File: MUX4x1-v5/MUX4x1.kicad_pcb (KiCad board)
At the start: 2 copper layers, 94 x 55.9 mm, 28 parts, among them J1 Screw_Terminal_01x02, J12 Conn_01x09_Male, J13 Conn_01x01_Male, J2 Conn_01x09_Male, J3 Conn_01x09_Male, J4 Conn_01x09_Male, J5 Conn_01x09_Male, J6 Conn_01x09_Male, J7 Conn_01x03_Male, U1 74LS153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

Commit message: MUX4:1 v5 in work
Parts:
- added C4: 0.1uF, Capacitor_SMD:C_0805_2012Metric_Pad1.18x1.45mm_HandSolder, F.Cu at (100.3, 134.6)
- added C5: 0.1uF, Capacitor_SMD:C_0805_2012Metric_Pad1.18x1.45mm_HandSolder, F.Cu at (85.1, 134.9)
- moved R1 4.72 mm to (145.4, 116.8), turned to 180 degrees
- moved H3 2.62 mm to (66.0, 155.6)
- moved H1 2.54 mm to (66.0, 109.2)
- moved H4 0.63 mm to (152.4, 155.6)
- moved C2 0.23 mm to (69.8, 133.6)
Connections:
- J7 pad 1: /S0 -> /S1
- J7 pad 2: /S1 -> /S0
- R2 pad 2: /S0 -> /S1
- R3 pad 2: /S1 -> /S0
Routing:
- net GND: track 0.00 -> 338.5 mm, vias 0 -> 1
- net VCC: track 0.00 -> 199.0 mm, vias 0 -> 5
- net /~E: track 0.00 -> 116.2 mm
- net /S1: track 0.00 -> 107.5 mm
- net /S0: track 0.00 -> 105.4 mm
- net /O0: track 0.00 -> 82.6 mm
- net /O2: track 0.00 -> 71.0 mm
- net /O1: track 0.00 -> 69.5 mm
- net /O3: track 0.00 -> 55.1 mm
- net /O4: track 0.00 -> 55.0 mm
- net /O5: track 0.00 -> 40.8 mm
- net /O6: track 0.00 -> 40.7 mm
- net /D7: track 0.00 -> 40.1 mm
- net /D0: track 0.00 -> 37.8 mm
- net /C7: track 0.00 -> 37.3 mm
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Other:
- board size 94 x 55.9 mm -> 96.5 x 56.5 mm

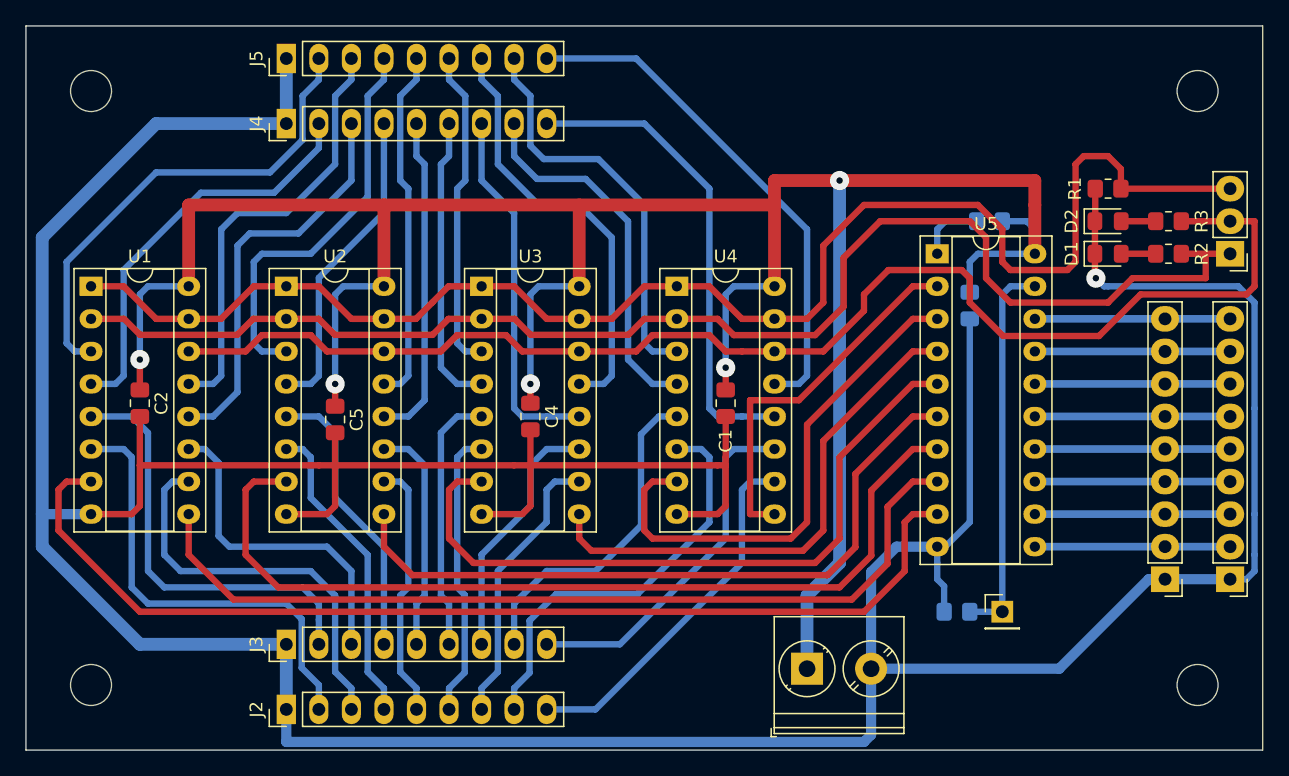
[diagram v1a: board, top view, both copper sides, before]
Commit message: MUX4:1 v5 polishing
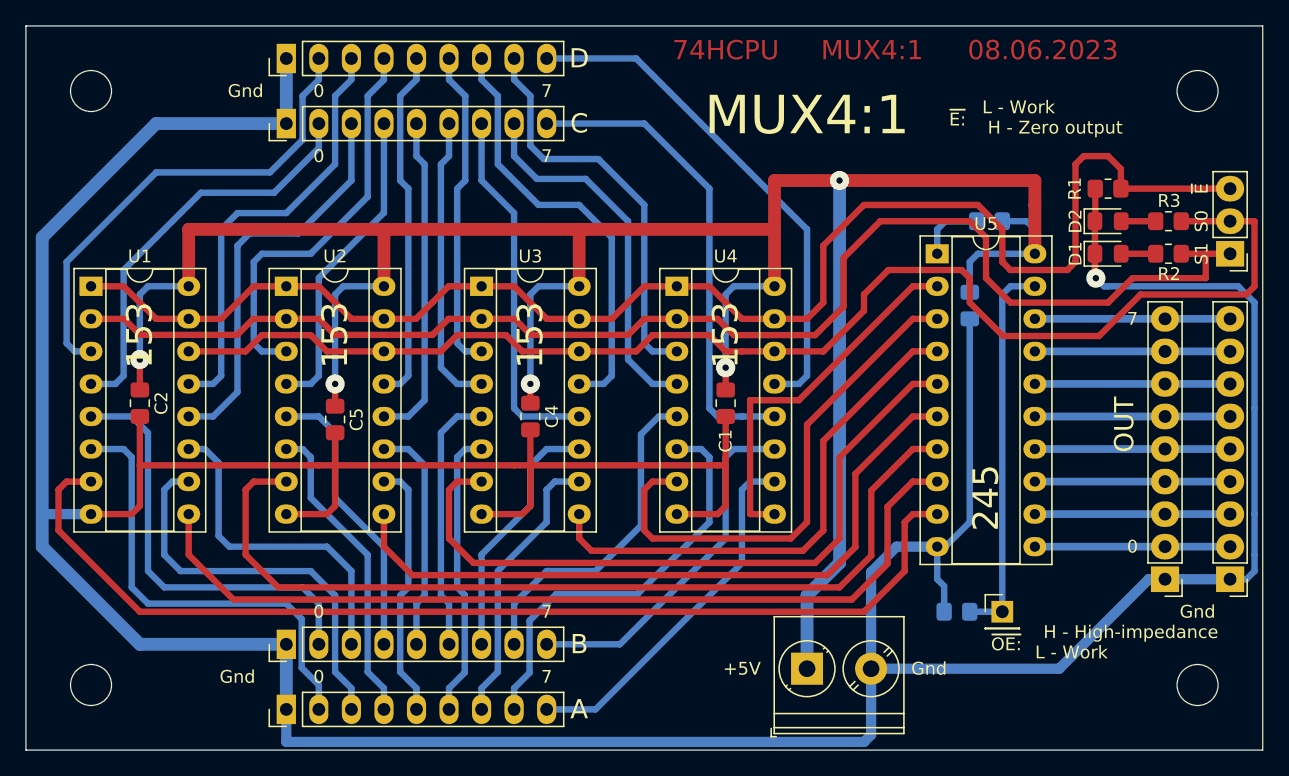
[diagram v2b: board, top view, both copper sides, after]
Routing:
- net VCC: track 199.0 -> 193.3 mm
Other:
- board text added: "+5V"
- board text added: "0"
- board text added: "08.06.2023"
- board text added: "153"
- board text added: "245"
- board text added: "7"
- board text added: "74HCPU"
- board text added: "A"
- board text added: "B"
- board text added: "C"
- board text added: "D"
- board text added: "Gnd"
- board text added: "H - High-impedance"
- board text added: "H - Zero output"
- board text added: "L - Work"
- board text added: "MUX4:1"
- board text added: "OUT"
- board text added: "S0"
- board text added: "S1"
- board text added: "~E"
- board text added: "~E:"
- board text added: "~OE:"

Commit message: Fix corners
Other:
- outline, holes or cut-outs redrawn
- board text added: "18.06.2023"
- board text removed: "08.06.2023"
